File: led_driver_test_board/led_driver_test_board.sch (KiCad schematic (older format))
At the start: 111 parts, among them P1 CONN_01X06_M50-3530642, P2 CONN_01X06_M50-3530642, P3 CONN_01X06_M50-3530642, P4 CONN_01X06_M50-3530642, Q1 Q_NMOS_SSM3K09FULF, Q2 Q_NMOS_SSM3K09FULF, Q3 Q_NMOS_SSM3K09FULF, Q4 Q_NMOS_SSM3K09FULF, Q5 Q_NMOS_SSM3K09FULF, Q6 Q_NMOS_SSM3K09FULF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

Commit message: Updated placeholder resistors in schematic
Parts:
- removed R10, R11, R12, R15, R16, R17, R18, R19, R20, R21, R22, R23, R4, R5, R6, R7, R8, R9: SMD-RES-0R-1_4W_0603_, Resistors_SMD:R_0603, symbol SMD-RES-0R-1_4W_0603_
- removed R40: CONNEX-SMD-RES-0-0603, Resistors_SMD:R_0603, symbol CONNEX-SMD-RES-0-0603
- added P4: CONN_01X06_M50-3530642, Pin_Headers:Pin_Header_Straight_1x06, symbol CONN_01X06_M50-3530642
- added R10, R21: CONNEX-SMD-RES-120-0603, R0603, symbol CONNEX-SMD-RES-120-0603
- added R11, R22: CONNEX-SMD-RES-60R4-0603, R0603, symbol CONNEX-SMD-RES-60R4-0603
- added R12, R23: CONNEX-SMD-RES-40R2-0603, R0603, symbol CONNEX-SMD-RES-40R2-0603
- added R15, R4: CONNEX-SMD-RES-20-0603, R0603, symbol CONNEX-SMD-RES-20-0603
- added R16, R20, R5, R9: CONNEX-SMD-RES-10-0603, R0603, symbol CONNEX-SMD-RES-10-0603
- added R17, R6: CONNEX-SMD-RES-6R65-0603, R0603, symbol CONNEX-SMD-RES-6R65-0603
- added R18, R7: CONNEX-SMD-RES-30-0603, R0603, symbol CONNEX-SMD-RES-30-0603
- added R19, R8: CONNEX-SMD-RES-15-0603, R0603, symbol CONNEX-SMD-RES-15-0603
- added R40: CONNEX-SMD-RES-4K02-0603, R0603, symbol CONNEX-SMD-RES-4K02-0603
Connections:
- net BOOT_RX: now also P4.5 (P5)
- net BOOT_TX: now also P4.6 (P6)
- net GND: now also P4.1 (P1), R40.1
- net LED_DRV_BLUE: now also R18.1, R19.1, R20.1, R7.1, R8.1, R9.1
- net LED_DRV_GREEN: now also R15.1, R16.1, R17.1, R4.1, R5.1, R6.1
- net LED_DRV_RED: now also R10.1, R11.1, R12.1, R21.1, R22.1, R23.1
- net RESET_N: now also P4.4 (P4)
- net at Q1.3 (D): now also R4.2, R5.2, R6.2
- net at Q2.3 (D): now also R7.2, R8.2, R9.2
- net at Q3.3 (D): now also R10.2, R11.2, R12.2
- net at Q4.3 (D): now also R15.2, R16.2, R17.2
- net at Q5.3 (D): now also R18.2, R19.2, R20.2
- net at Q6.3 (D): now also R21.2, R22.2, R23.2
- net at U2.4 (PROG): now also R40.2

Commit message: Changed boot tx/rx on connector. Annotated
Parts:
- R10, R11, R12, R15, R16, R17, R18, R19, R20, R21, R22, R23, R4, R40, R5, R6, R7, R8, R9: footprint R0603 -> Resistors_SMD:R_0603
- renumbered P4 to P5
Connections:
- net BOOT_RX: now also P5.6 (P6); no longer P5.5 (P5)
- net BOOT_TX: now also P5.5 (P5); no longer P5.6 (P6)
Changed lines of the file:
@@
 F 0 "R40" V 9495 1895 45  0000 L BNN
 F 1 "CONNEX-SMD-RES-4K02-0603" H 9175 2325 20  0001 L BNN
-F 2 "R0603" H 9400 2025 20  0001 C CNN
+F 2 "Resistors_SMD:R_0603" H 9400 2025 20  0001 C CNN
 F 3 "N/A" H 9400 1975 20  0001 C CNN
 F 4 "https://www.digikey.com/product-detail/en/vishay-dale/CRCW06034K02FKEA/541-4.02KHCT-ND/1179877" H 9400 2075 20  0001 C CNN "LINK"
@@
 F 0 "R15" H 2200 4350 45  0000 L BNN
 F 1 "CONNEX-SMD-RES-20-0603" H 2200 4875 20  0001 L BNN
-F 2 "R0603" H 2400 4575 20  0001 C CNN
+F 2 "Resistors_SMD:R_0603" H 2400 4575 20  0001 C CNN
 F 3 "N/A" H 2400 4525 20  0001 C CNN
 F 4 "https://www.digikey.com/product-detail/en/vishay-dale/CRCW060320R0JNEA/541-20GCT-ND/1179328" H 2400 4625 20  0001 C CNN "LINK"
@@
 F 0 "R4" H 2250 2700 45  0000 L BNN
 F 1 "CONNEX-SMD-RES-20-0603" H 2200 3225 20  0001 L BNN
-F 2 "R0603" H 2400 2925 20  0001 C CNN
+F 2 "Resistors_SMD:R_0603" H 2400 2925 20  0001 C CNN
 F 3 "N/A" H 2400 2875 20  0001 C CNN
 F 4 "https://www.digikey.com/product-detail/en/vishay-dale/CRCW060320R0JNEA/541-20GCT-ND/1179328" H 2400 2975 20  0001 C CNN "LINK"
@@
 F 0 "R5" H 2350 2700 45  0000 L BNN
 F 1 "CONNEX-SMD-RES-10-0603" H 2275 3225 20  0001 L BNN
-F 2 "R0603" H 2500 2925 20  0001 C CNN
+F 2 "Resistors_SMD:R_0603" H 2500 2925 20  0001 C CNN
 F 3 "N/A" H 2500 2875 20  0001 C CNN
 F 4 "https://www.digikey.com/product-detail/en/vishay-dale/RCA060310R0JNEA/541-2212-1-ND/4946865" H 2500 2975 20  0001 C CNN "LINK"
@@
 F 0 "R16" H 2300 4350 45  0000 L BNN
 F 1 "CONNEX-SMD-RES-10-0603" H 2275 4875 20  0001 L BNN
-F 2 "R0603" H 2500 4575 20  0001 C CNN
+F 2 "Resistors_SMD:R_0603" H 2500 4575 20  0001 C CNN
 F 3 "N/A" H 2500 4525 20  0001 C CNN
 F 4 "https://www.digikey.com/product-detail/en/vishay-dale/RCA060310R0JNEA/541-2212-1-ND/4946865" H 2500 4625 20  0001 C CNN "LINK"
@@
 F 0 "R17" H 2400 4350 45  0000 L BNN
 F 1 "CONNEX-SMD-RES-6R65-0603" H 2375 4875 20  0001 L BNN
-F 2 "R0603" H 2600 4575 20  0001 C CNN
+F 2 "Resistors_SMD:R_0603" H 2600 4575 20  0001 C CNN
 F 3 "N/A" H 2600 4525 20  0001 C CNN
 F 4 "https://www.digikey.com/product-detail/en/vishay-dale/CRCW06036R65FKEA/541-6.65HHCT-ND/1962091" H 2600 4625 20  0001 C CNN "LINK"
@@
 F 0 "R6" H 2450 2700 45  0000 L BNN
 F 1 "CONNEX-SMD-RES-6R65-0603" H 2375 3225 20  0001 L BNN
-F 2 "R0603" H 2600 2925 20  0001 C CNN
+F 2 "Resistors_SMD:R_0603" H 2600 2925 20  0001 C CNN
 F 3 "N/A" H 2600 2875 20  0001 C CNN
 F 4 "https://www.digikey.com/product-detail/en/vishay-dale/CRCW06036R65FKEA/541-6.65HHCT-ND/1962091" H 2600 2975 20  0001 C CNN "LINK"
@@
 F 0 "R9" H 3500 2700 45  0000 L BNN
 F 1 "CONNEX-SMD-RES-10-0603" H 3425 3225 20  0001 L BNN
-F 2 "R0603" H 3650 2925 20  0001 C CNN
+F 2 "Resistors_SMD:R_0603" H 3650 2925 20  0001 C CNN
 F 3 "N/A" H 3650 2875 20  0001 C CNN
 F 4 "https://www.digikey.com/product-detail/en/vishay-dale/RCA060310R0JNEA/541-2212-1-ND/4946865" H 3650 2975 20  0001 C CNN "LINK"
@@
 F 0 "R20" H 3450 4350 45  0000 L BNN
 F 1 "CONNEX-SMD-RES-10-0603" H 3425 4875 20  0001 L BNN
-F 2 "R0603" H 3650 4575 20  0001 C CNN
+F 2 "Resistors_SMD:R_0603" H 3650 4575 20  0001 C CNN
 F 3 "N/A" H 3650 4525 20  0001 C CNN
 F 4 "https://www.digikey.com/product-detail/en/vishay-dale/RCA060310R0JNEA/541-2212-1-ND/4946865" H 3650 4625 20  0001 C CNN "LINK"
@@
 F 0 "R18" H 3250 4350 45  0000 L BNN
 F 1 "CONNEX-SMD-RES-30-0603" H 3225 4875 20  0001 L BNN
-F 2 "R0603" H 3450 4575 20  0001 C CNN
+F 2 "Resistors_SMD:R_0603" H 3450 4575 20  0001 C CNN
 F 3 "N/A" H 3450 4525 20  0001 C CNN
 F 4 "https://www.digikey.com/product-detail/en/vishay-dale/CRCW060330R0JNEA/541-30GCT-ND/1179332" H 3450 4625 20  0001 C CNN "LINK"
@@
 F 0 "R19" H 3350 4350 45  0000 L BNN
 F 1 "CONNEX-SMD-RES-15-0603" H 3325 4875 20  0001 L BNN
-F 2 "R0603" H 3550 4575 20  0001 C CNN
+F 2 "Resistors_SMD:R_0603" H 3550 4575 20  0001 C CNN
 F 3 "N/A" H 3550 4525 20  0001 C CNN
 F 4 "https://www.digikey.com/product-detail/en/vishay-dale/CRCW060315R0JNEA/541-15GCT-ND/1179325" H 3550 4625 20  0001 C CNN "LINK"
@@
 F 0 "R8" H 3400 2700 45  0000 L BNN
 F 1 "CONNEX-SMD-RES-15-0603" H 3325 3225 20  0001 L BNN
-F 2 "R0603" H 3550 2925 20  0001 C CNN
+F 2 "Resistors_SMD:R_0603" H 3550 2925 20  0001 C CNN
 F 3 "N/A" H 3550 2875 20  0001 C CNN
 F 4 "https://www.digikey.com/product-detail/en/vishay-dale/CRCW060315R0JNEA/541-15GCT-ND/1179325" H 3550 2975 20  0001 C CNN "LINK"
@@
 F 0 "R7" H 3300 2700 45  0000 L BNN
 F 1 "CONNEX-SMD-RES-30-0603" H 3225 3225 20  0001 L BNN
-F 2 "R0603" H 3450 2925 20  0001 C CNN
+F 2 "Resistors_SMD:R_0603" H 3450 2925 20  0001 C CNN
 F 3 "N/A" H 3450 2875 20  0001 C CNN
 F 4 "https://www.digikey.com/product-detail/en/vishay-dale/CRCW060330R0JNEA/541-30GCT-ND/1179332" H 3450 2975 20  0001 C CNN "LINK"
@@
 F 0 "R10" H 4350 2700 45  0000 L BNN
 F 1 "CONNEX-SMD-RES-120-0603" H 4325 3225 20  0001 L BNN
-F 2 "R0603" H 4550 2925 20  0001 C CNN
+F 2 "Resistors_SMD:R_0603" H 4550 2925 20  0001 C CNN
 F 3 "N/A" H 4550 2875 20  0001 C CNN
 F 4 "https://www.digikey.com/product-detail/en/vishay-dale/CRCW0603120RJNEA/541-120GCT-ND/1179347" H 4550 2975 20  0001 C CNN "LINK"
@@
 F 0 "R11" H 4450 2700 45  0000 L BNN
 F 1 "CONNEX-SMD-RES-60R4-0603" H 4425 3225 20  0001 L BNN
-F 2 "R0603" H 4650 2925 20  0001 C CNN
+F 2 "Resistors_SMD:R_0603" H 4650 2925 20  0001 C CNN
 F 3 "N/A" H 4650 2875 20  0001 C CNN
 F 4 "https://www.digikey.com/product-detail/en/vishay-dale/CRCW060360R4FKEA/541-60.4HCT-ND/1179670" H 4650 2975 20  0001 C CNN "LINK"
@@
 F 0 "R12" H 4550 2700 45  0000 L BNN
 F 1 "CONNEX-SMD-RES-40R2-0603" H 4525 3225 20  0001 L BNN
-F 2 "R0603" H 4750 2925 20  0001 C CNN
+F 2 "Resistors_SMD:R_0603" H 4750 2925 20  0001 C CNN
 F 3 "N/A" H 4750 2875 20  0001 C CNN
 F 4 "https://www.digikey.com/product-detail/en/vishay-dale/CRCW060340R2FKEA/541-40.2HCT-ND/1179649" H 4750 2975 20  0001 C CNN "LINK"
@@
 F 0 "R21" H 4350 4350 45  0000 L BNN
 F 1 "CONNEX-SMD-RES-120-0603" H 4325 4875 20  0001 L BNN
-F 2 "R0603" H 4550 4575 20  0001 C CNN
+F 2 "Resistors_SMD:R_0603" H 4550 4575 20  0001 C CNN
 F 3 "N/A" H 4550 4525 20  0001 C CNN
 F 4 "https://www.digikey.com/product-detail/en/vishay-dale/CRCW0603120RJNEA/541-120GCT-ND/1179347" H 4550 4625 20  0001 C CNN "LINK"
@@
 F 0 "R22" H 4450 4350 45  0000 L BNN
 F 1 "CONNEX-SMD-RES-60R4-0603" H 4425 4875 20  0001 L BNN
-F 2 "R0603" H 4650 4575 20  0001 C CNN
+F 2 "Resistors_SMD:R_0603" H 4650 4575 20  0001 C CNN
 F 3 "N/A" H 4650 4525 20  0001 C CNN
 F 4 "https://www.digikey.com/product-detail/en/vishay-dale/CRCW060360R4FKEA/541-60.4HCT-ND/1179670" H 4650 4625 20  0001 C CNN "LINK"
@@
 F 0 "R23" H 4550 4350 45  0000 L BNN
 F 1 "CONNEX-SMD-RES-40R2-0603" H 4525 4875 20  0001 L BNN
-F 2 "R0603" H 4750 4575 20  0001 C CNN
+F 2 "Resistors_SMD:R_0603" H 4750 4575 20  0001 C CNN
 F 3 "N/A" H 4750 4525 20  0001 C CNN
 F 4 "https://www.digikey.com/product-detail/en/vishay-dale/CRCW060340R2FKEA/541-40.2HCT-ND/1179649" H 4750 4625 20  0001 C CNN "LINK"
@@
 $EndComp
 $Comp
-L CONN_01X06_M50-3530642 P4
+L CONN_01X06_M50-3530642 P5
 U 1 1 5A30A0BE
 P 4350 7250
-F 0 "P4" H 4350 7600 50  0000 C CNN
+F 0 "P5" H 4350 7600 50  0000 C CNN
 F 1 "CONN_01X06_M50-3530642" V 4450 7250 50  0001 C CNN
 F 2 "Pin_Headers:Pin_Header_Straight_1x06" H 4350 7250 50  0001 C CNN
@@
 $EndComp
 $Comp
-L GND #PWR?
+L GND #PWR038
 U 1 1 5A30AE55
 P 4050 7575
-F 0 "#PWR?" H 4050 7325 50  0001 C CNN
+F 0 "#PWR038" H 4050 7325 50  0001 C CNN
 F 1 "GND" H 4050 7425 50  0000 C CNN
 F 2 "" H 4050 7575 50  0000 C CNN
@@
 Wire Wire Line
 	4150 7000 3075 7000
-Text Label 3075 7000 0    60   ~ 0
+Text Label 3100 7100 0    60   ~ 0
 BOOT_TX
 Wire Wire Line
 	4150 7100 3075 7100
-Text Label 3075 7100 0    60   ~ 0
+Text Label 3100 7000 0    60   ~ 0
 BOOT_RX
 Wire Wire Line

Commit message: Finished first round of routing, passes DRC
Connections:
- net +3V3: now also P5.2 (P2)
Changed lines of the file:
@@
 Text Label 3075 7200 0    60   ~ 0
 RESET_N
+$Comp
+L +3.3V #PWR?
+U 1 1 5A2DAA30
+P 4000 7400
+F 0 "#PWR?" H 4000 7250 50  0001 C CNN
+F 1 "+3.3V" V 4000 7650 50  0000 C CNN
+F 2 "" H 4000 7400 50  0000 C CNN
+F 3 "" H 4000 7400 50  0000 C CNN
+	1    4000 7400
+	0    -1   -1   0
+$EndComp
+Wire Wire Line
+	4000 7400 4150 7400
 $EndSCHEMATC

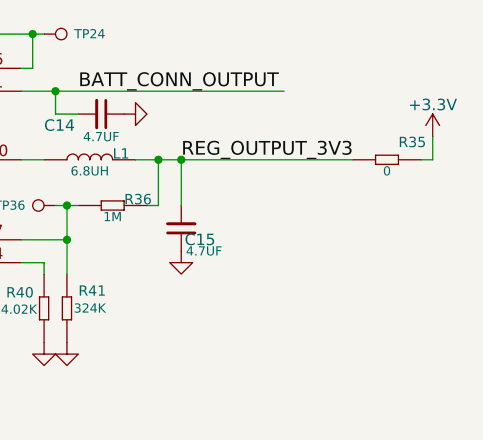
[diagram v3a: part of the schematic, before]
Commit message: Replaced R35 with correct BOM
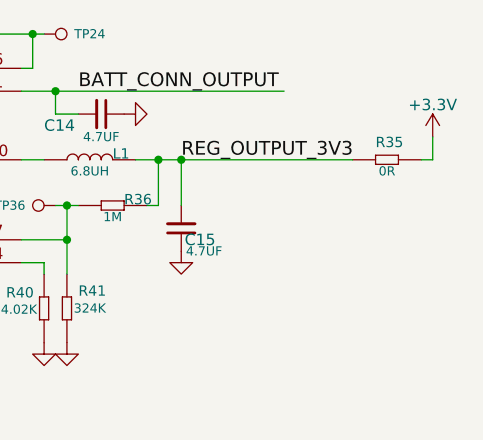
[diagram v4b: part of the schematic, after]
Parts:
- removed R35: CONNEX-SMD-RES-0-0603, Resistors_SMD:R_0603, symbol CONNEX-SMD-RES-0-0603
- added R35: SMD-RES-0R-1_4W_0603_, Resistors_SMD:R_0603, symbol SMD-RES-0R-1_4W_0603_
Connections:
- net +3V3: now also R35.2
- net REG_OUTPUT_3V3: now also R35.1
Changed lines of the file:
@@
 $EndComp
 Connection ~ 9350 650
-$Comp
-L CONNEX-SMD-RES-0-0603 R35
-U 1 1 5A2D981F
-P 10900 1200
-F 0 "R35" H 10950 1250 45  0000 L BNN
-F 1 "CONNEX-SMD-RES-0-0603" H 10700 1675 20  0001 L BNN
-F 2 "Resistors_SMD:R_0603" H 10900 1375 20  0001 C CNN
-F 3 "N/A" H 10900 1325 20  0001 C CNN
-F 4 "https://www.digikey.com/product-detail/en/vishay-dale/CRCW06030000Z0EAHP/541-0.0SBCT-ND/2222749" H 10900 1425 20  0001 C CNN "LINK"
-F 5 "YES" H 10800 1250 20  0001 C CNN "PLACE"
-F 6 "CRCW06030000Z0EAHP" H 10900 1575 20  0001 C CNN "MPN"
-F 7 "VISHAY DALE" H 10900 1625 20  0001 C CNN "MANUFACTURER"
-F 8 "DIGIKEY" H 10900 1525 20  0001 C CNN "SUPPLIER"
-F 9 "0" H 10900 1150 40  0000 C CNN "RESISTANCE"
-F 10 "541-0.0SBCT-ND" H 10900 1475 20  0001 C CNN "SUPPLIER PART"
-	1    10900 1200
-	1    0    0    -1
-$EndComp
 Text Label 10000 1200 0    60   ~ 0
 REG_OUTPUT_3V3
@@
 RESET_N
 $Comp
-L +3.3V #PWR?
+L +3.3V #PWR039
 U 1 1 5A2DAA30
 P 4000 7400
-F 0 "#PWR?" H 4000 7250 50  0001 C CNN
+F 0 "#PWR039" H 4000 7250 50  0001 C CNN
 F 1 "+3.3V" V 4000 7650 50  0000 C CNN
 F 2 "" H 4000 7400 50  0000 C CNN
@@
 Wire Wire Line
 	4000 7400 4150 7400
+$Comp
+L SMD-RES-0R-1_4W_0603_ R35
+U 1 1 5A2E1E2C
+P 10900 1200
+F 0 "R35" H 10850 1250 45  0000 L BNN
+F 1 "SMD-RES-0R-1_4W_0603_" H 10825 1450 45  0001 L BNN
+F 2 "Resistors_SMD:R_0603" H 10900 1200 40  0001 C CNN
+F 3 "" H 10750 1250 40  0001 C CNN
+F 4 "0.15" H 11450 1950 60  0001 C CNN "COST (1X)"
+F 5 "541-0.0SBCT-ND" H 11250 1750 60  0001 C CNN "SUPPLIER PART"
+F 6 "DIGIKEY" H 11150 1650 60  0001 C CNN "SUPPLIER"
+F 7 "https://www.digikey.com/product-detail/en/vishay-dale/CRCW06030000Z0EAHP/541-0.0SBCT-ND/2222749" H 11350 1850 60  0001 C CNN "LINK"
+F 8 "VISHAY DALE" H 11050 1550 60  0001 C CNN "MANUFACTURER"
+F 9 "YES" H 11050 1325 60  0001 C CNN "PLACE"
+F 10 "CRCW06030000Z0EAHP" H 11050 1400 20  0001 C CNN "MPN"
+F 11 "0R" H 10900 1150 40  0000 C CNN "RESISTANCE"
+F 12 "0603" H 10925 1100 40  0001 C CNN "FP"
+	1    10900 1200
+	1    0    0    -1
+$EndComp
 $EndSCHEMATC

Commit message: Minor changes to schematic
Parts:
- removed C1, C2: connex_cap_100NF_0603_10V, Capacitors_SMD:C_0603, symbol connex_cap_100NF_0603_10V
- added C1, C2: CONNEX-SMD-CAP-10NF-0603, 0603, symbol CONNEX-SMD-CAP-10NF-0603
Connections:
- net GND: now also C1.2, C2.2
- net at C3.1, R13.2, U1.19 (AVDD_1)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: now also C1.1, C2.1
- no-connect marks 0 -> 1

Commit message: Minor changes
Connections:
- net LED_RED: no longer TP6.1
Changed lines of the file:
@@
 	1800 1500 1800 1750
 Connection ~ 1800 1750
-Wire Wire Line
-	1850 1500 1850 1850
 Connection ~ 1850 1850
 Wire Wire Line

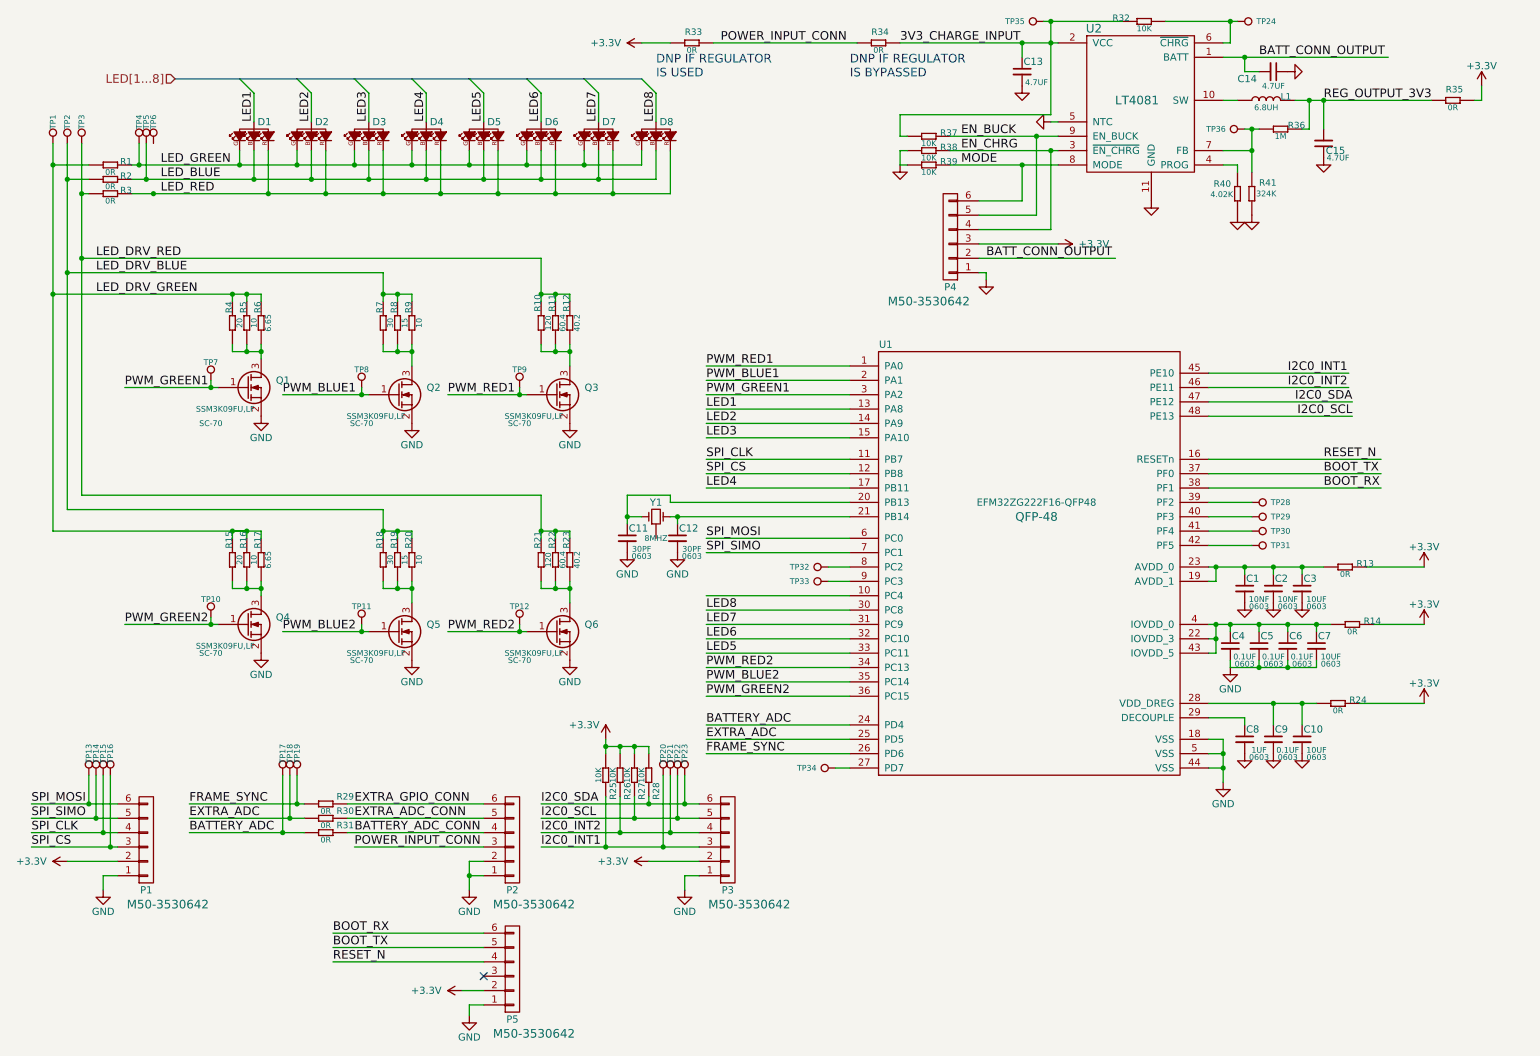
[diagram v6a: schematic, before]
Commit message: Version 1.1 - Unreveiwed - updated footprints for leds, crystal regulator, general layout, font sizes for labels
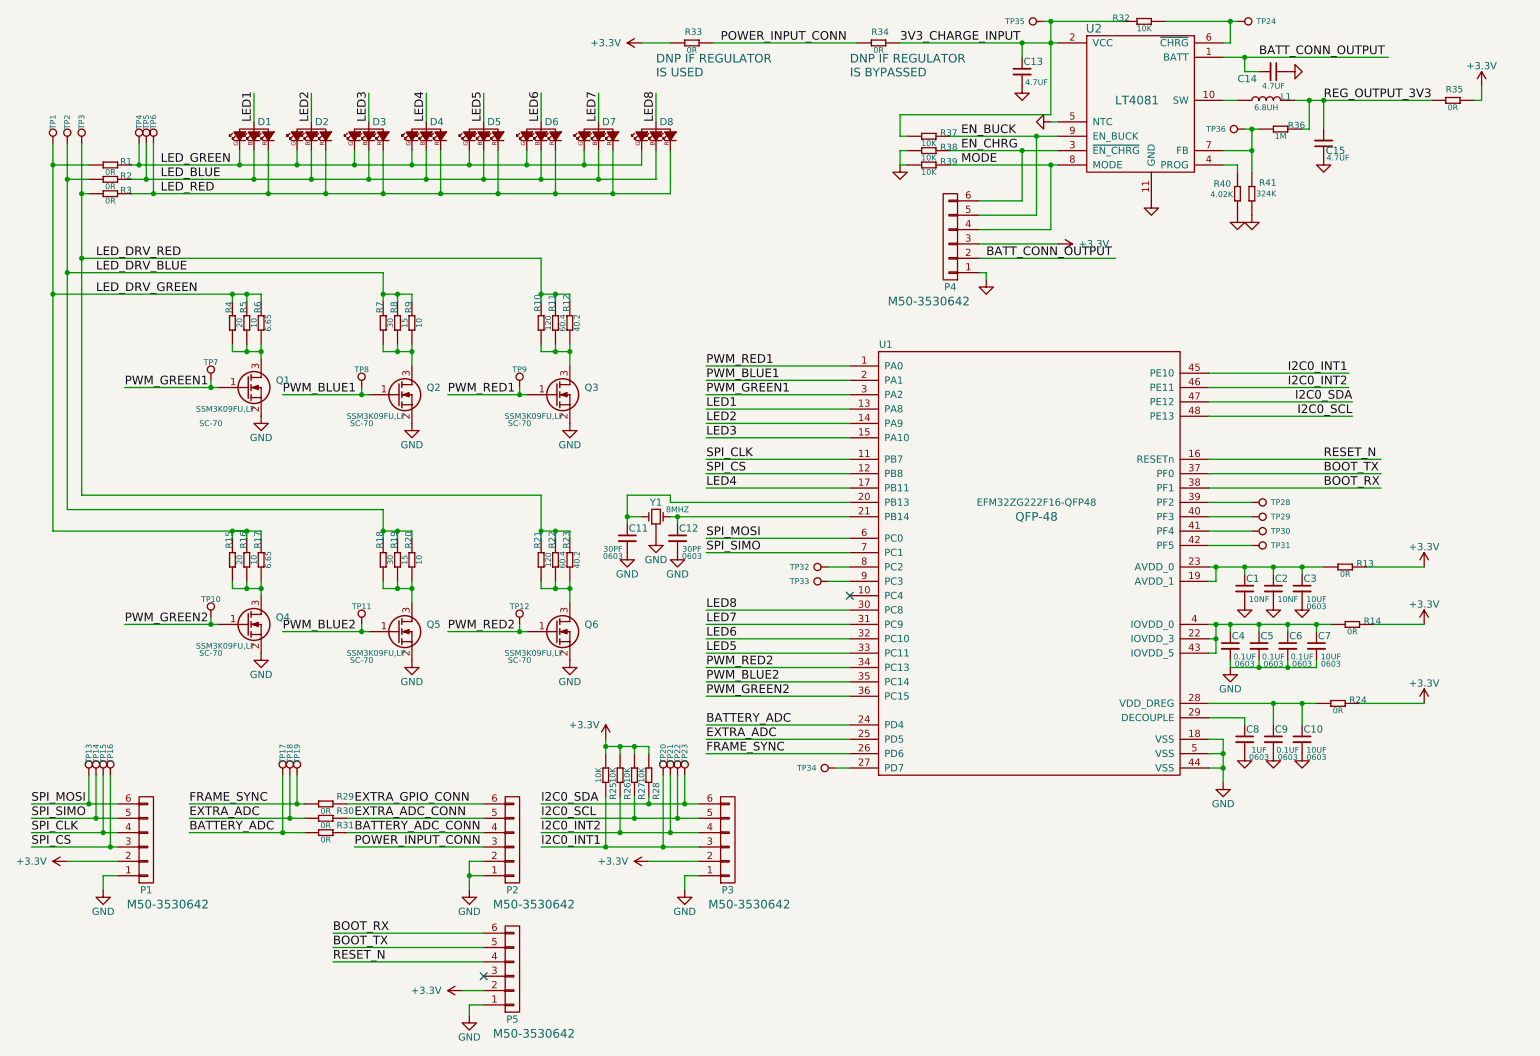
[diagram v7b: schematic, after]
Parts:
- C1, C2: footprint 0603 -> Capacitors_SMD:C_0603
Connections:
- net labels removed: LED[1...8]
- wire segments 389 -> 279
- no-connect marks 1 -> 2
